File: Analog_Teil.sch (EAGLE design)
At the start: 148 parts, among them J1 35RASMT2BHNTRX, J2 35RASMT2BHNTRX, T11 OPA388, T12 OPA388, T21 OPA388, T22 OPA388

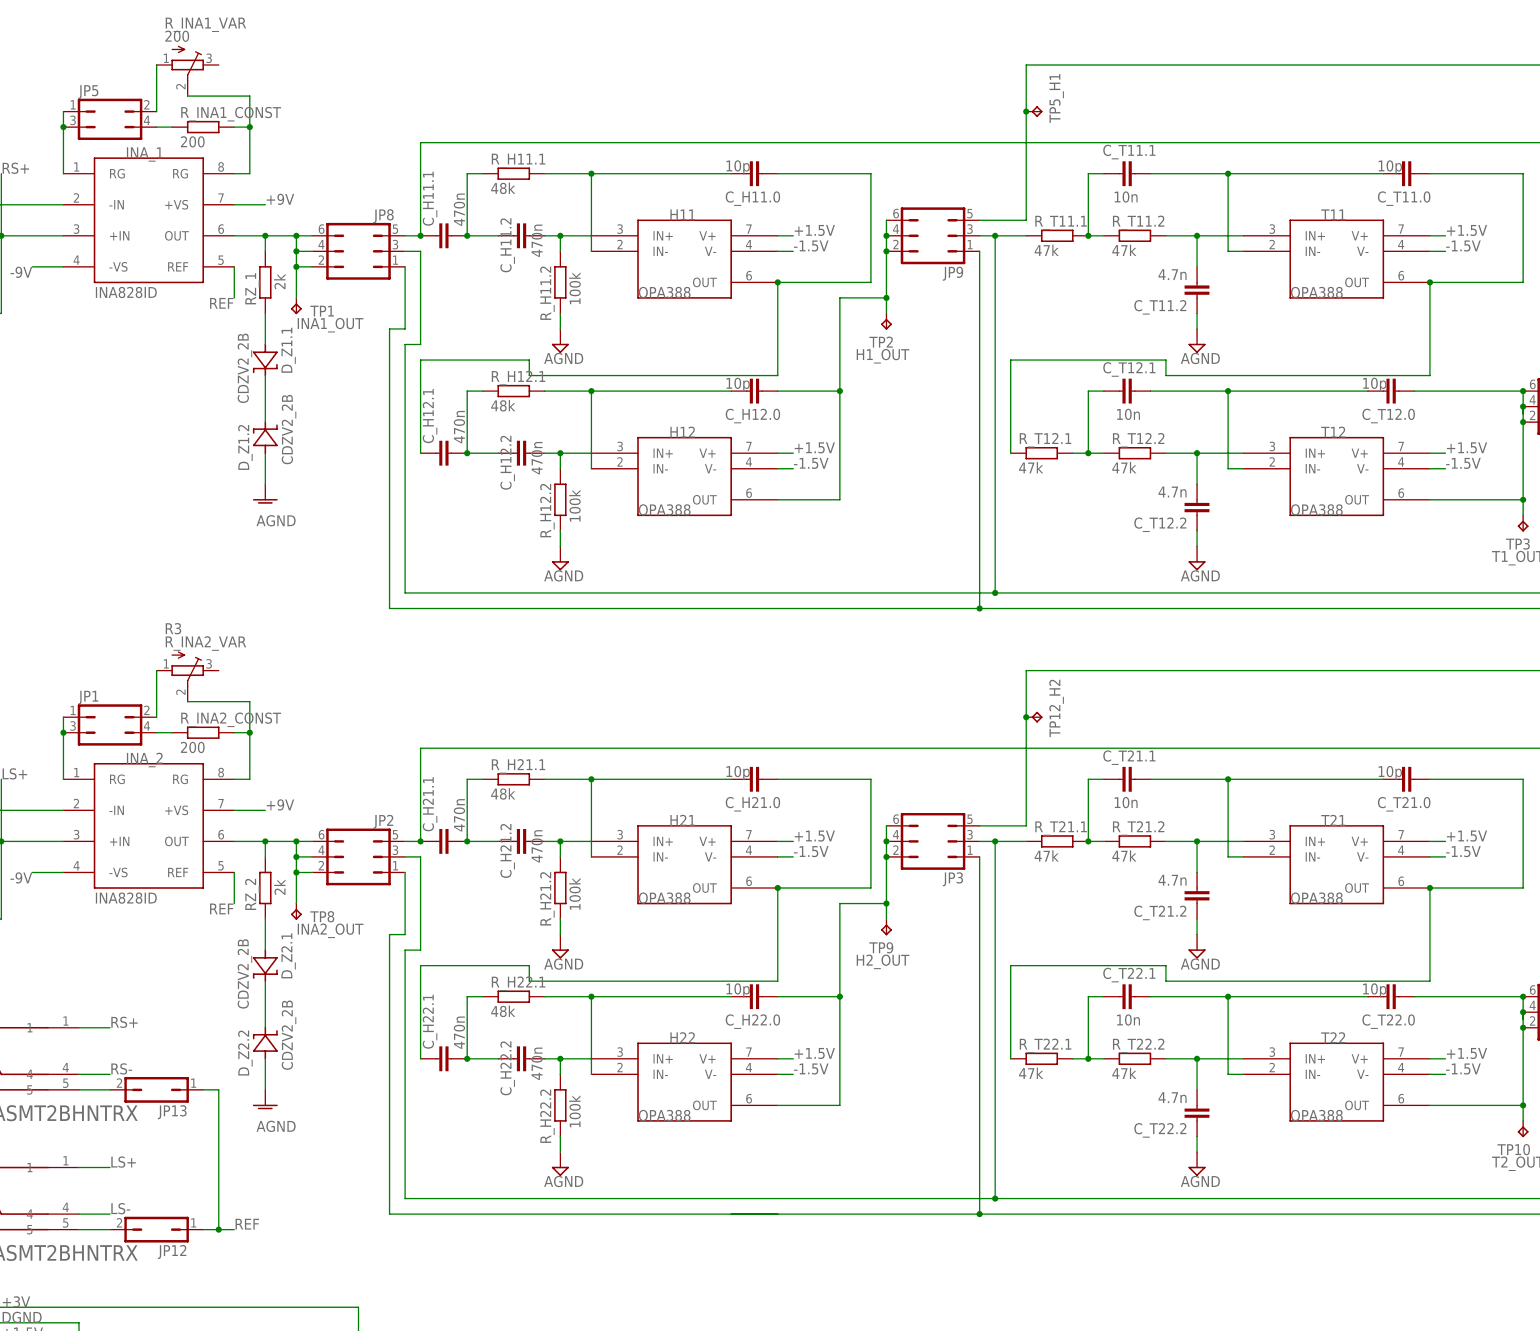
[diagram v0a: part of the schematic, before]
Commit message: Testpunkte, Widerstand hinter Poti, zusätzlich noch Power Supply Platine
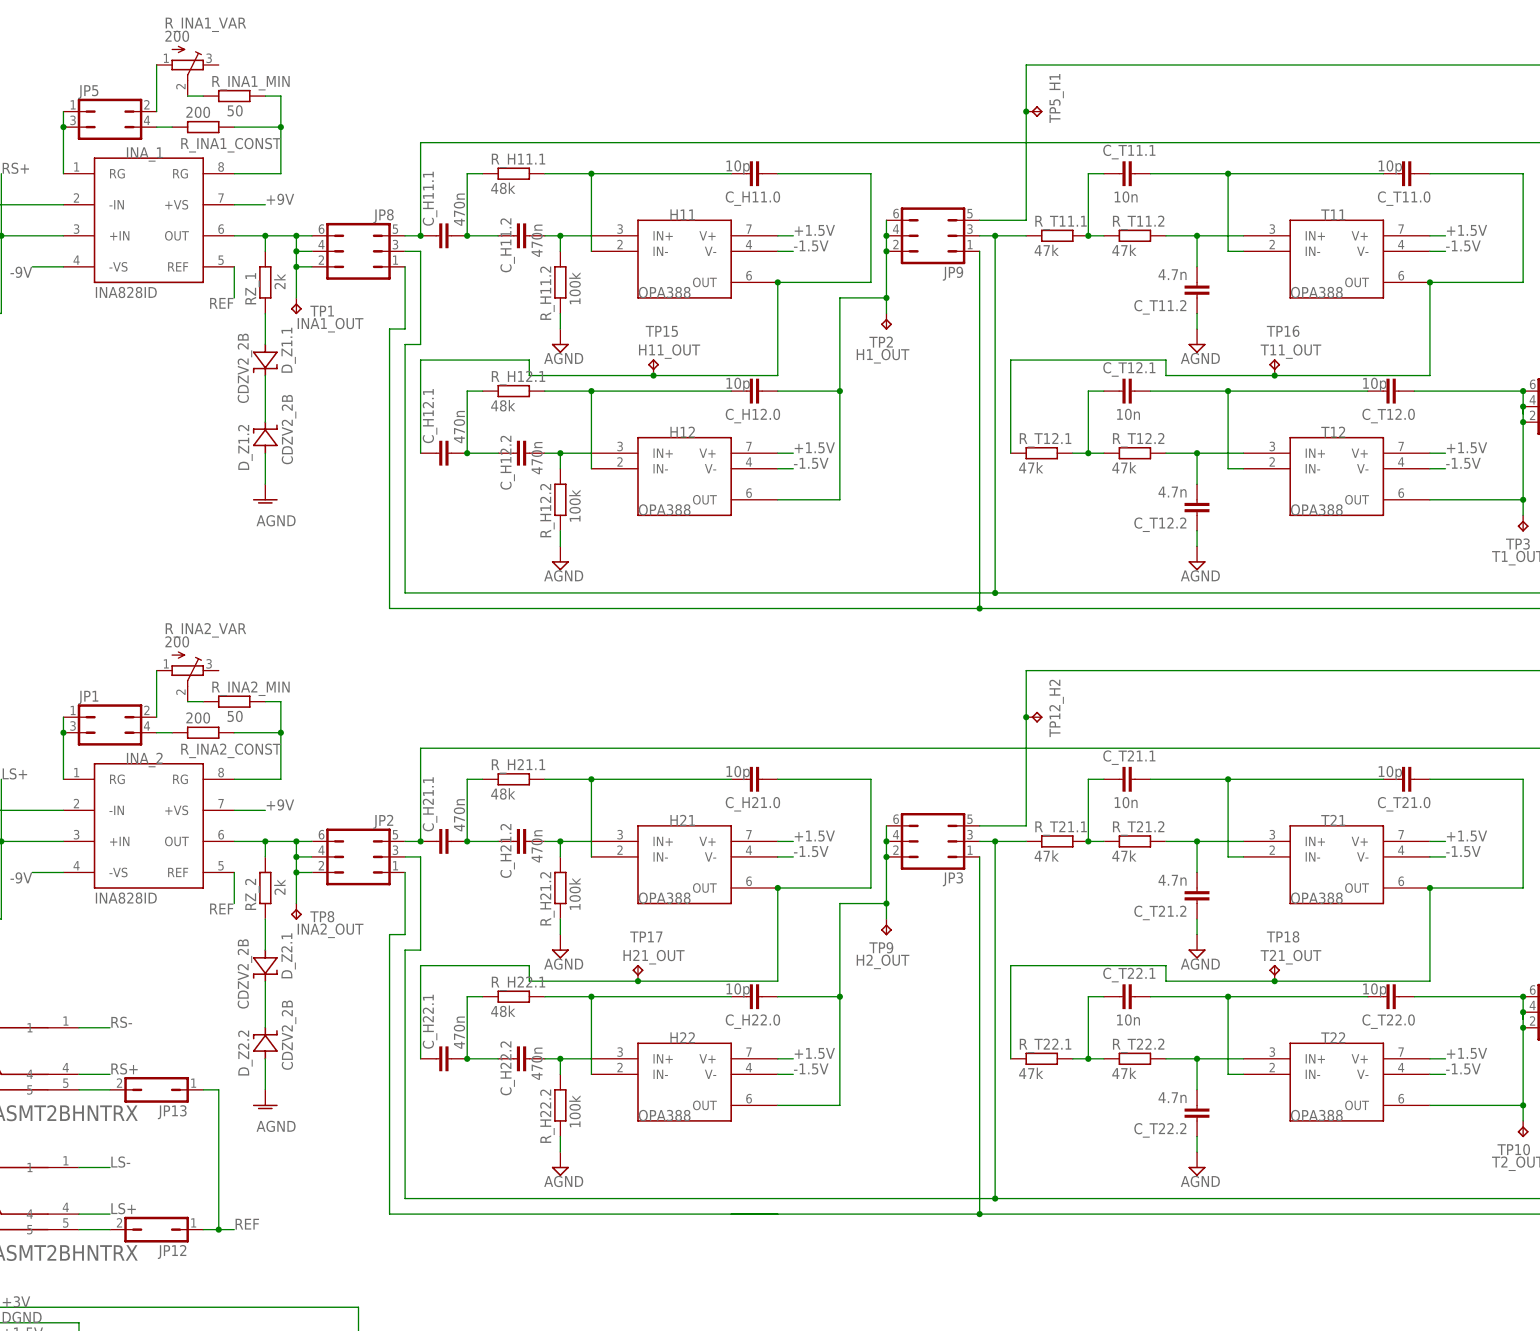
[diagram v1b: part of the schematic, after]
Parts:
- added R_INA1_MIN, R_INA2_MIN: 50, rcl:R-EU_R0805
- added TP15, TP16, TP17, TP18: TPPAD1-13, testpad:TPPAD1-13
- R_INA2_VAR: value R_INA2_VAR -> 200
- renumbered R3 to R_INA2_VAR
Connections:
- net N$1 renamed RG1+
- net N$38 renamed RG2+
- removed net N$2: INA_1.RG@2, R_INA1_CONST.2, R_INA1_VAR.S
- removed net N$23: INA_2.RG@2, R_INA2_CONST.2, R_INA2_VAR.S
- removed net N$46: C_H21.0.1, C_H22.1.1, H21.OUT
- removed net N$47: C_H11.0.1, C_H12.1.1, H11.OUT
- removed net N$48: C_T21.0.1, R_T22.1.1, T21.OUT
- removed net N$53: C_T11.0.1, R_T12.1.1, T11.OUT
- new net H11_OUT: C_H11.0.1, C_H12.1.1, H11.OUT, TP15.TP
- new net H21_OUT: C_H21.0.1, C_H22.1.1, H21.OUT, TP17.TP
- new net N$1: R_INA2_MIN.1, R_INA2_VAR.S
- new net N$54: R_INA1_MIN.1, R_INA1_VAR.S
- new net RG1-: INA_1.RG@2, R_INA1_CONST.2, R_INA1_MIN.2
- new net RG2-: INA_2.RG@2, R_INA2_CONST.2, R_INA2_MIN.2
- new net T11_OUT: C_T11.0.1, R_T12.1.1, T11.OUT, TP16.TP
- new net T21_OUT: C_T21.0.1, R_T22.1.1, T21.OUT, TP18.TP
- net LS+: now also J2.4; no longer J2.1
- net LS-: now also J2.1; no longer J2.4
- net RS+: now also J1.4; no longer J1.1
- net RS-: now also J1.1; no longer J1.4

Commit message: Schönheitsanpassungen
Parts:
- removed C_INA2+1, C_INA2-1: 100n, rcl:C-EUC0805
- added C_INA2+, C_INA2-: 100n, rcl:C-EUC0805
- R_LS1, R_RS: value 1Meg -> 10Meg
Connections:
- net +9V: now also C_INA2+.1; no longer C_INA2+1.1
- net -9V: now also C_INA2-.1; no longer C_INA2-1.1
- net AGND: now also C_INA2+.2, C_INA2-.2; no longer C_INA2+1.2, C_INA2-1.2
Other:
- note added: "Lowpass 500 Hz"
- note added: "bypass-capacitors"
- note added: "highpass 5 Hz"
- note added: "muscle-input"
- note added: "notchfilter 50 Hz"
- moved on the sheet: C+1.5, C+3, C+9, C-1.5, C_-9, C_H11+, C_H11-, C_H11.0, C_H11.1, C_H11.2, C_H12+, C_H12-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
